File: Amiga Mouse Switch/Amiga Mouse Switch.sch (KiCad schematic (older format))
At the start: 8 parts, among them J1 Joystick 0, J2 Joystick 1, M1 Mounting, M2 Mounting, M3 Mounting, M4 Mounting, M5 Mounting, M6 Mounting

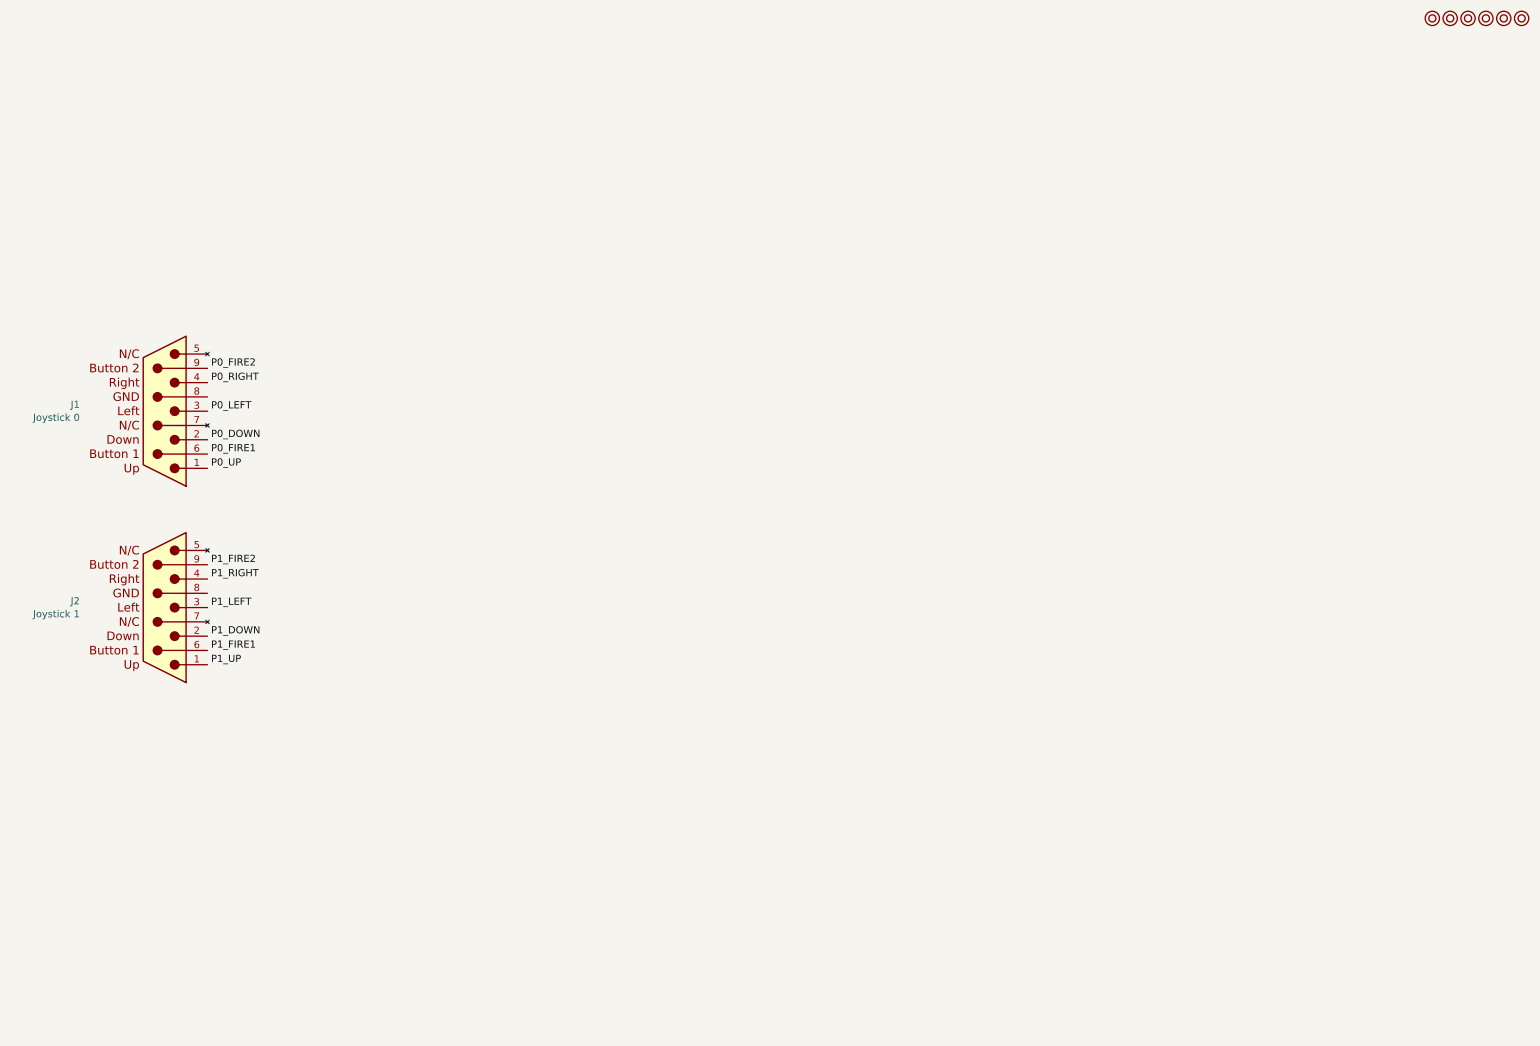
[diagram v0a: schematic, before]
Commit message: Schematic done
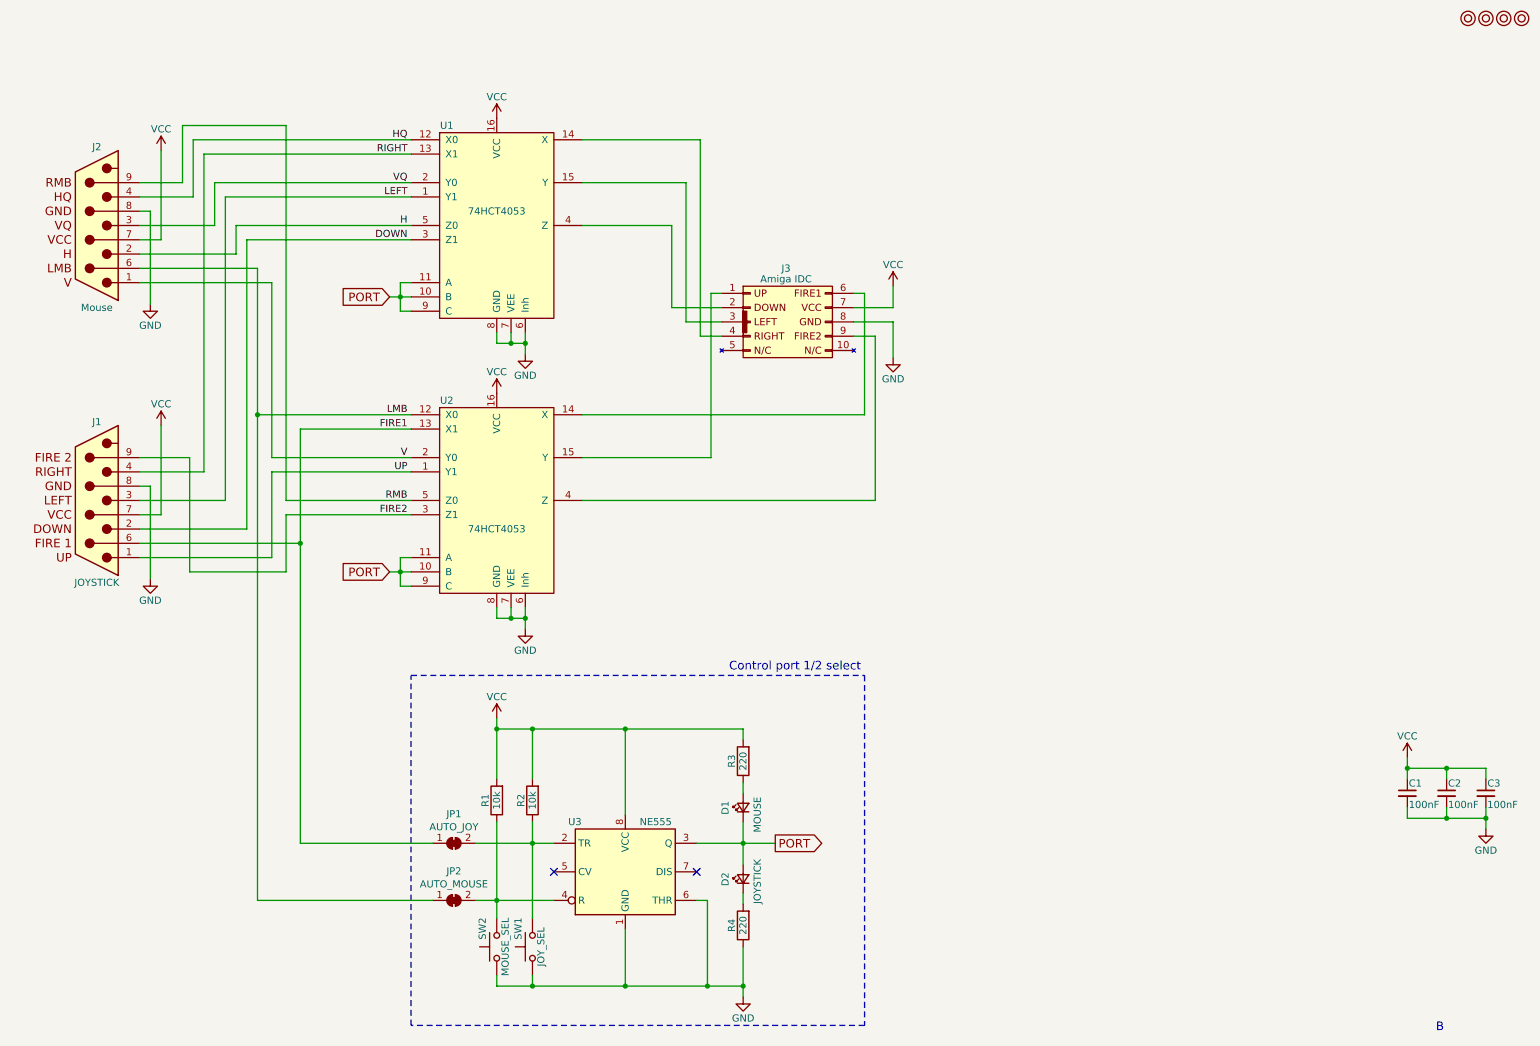
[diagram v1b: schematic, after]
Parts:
- removed J1: Joystick 0, RND:DSUB-9_Male_Horizontal_P2.77x2.84mm_EdgePinOffset7.70mm_Housed_MountingHolesOffset9.12mm, symbol sega_joypad:sms_joypad
- removed J2: Joystick 1, RND:DSUB-9_Male_Horizontal_P2.77x2.84mm_EdgePinOffset7.70mm_Housed_MountingHolesOffset9.12mm, symbol sega_joypad:sms_joypad
- removed M5, M6: Mounting, mounting:M3_pin, symbol mounting:Mounting
- added C1, C2, C3: 100nF, Capacitors_THT:C_Disc_D4.7mm_W2.5mm_P5.00mm, symbol Device:C_Small
- added D1: MOUSE, LEDs:LED_D5.0mm, symbol Device:LED_Small
- added D2: JOYSTICK, LEDs:LED_D5.0mm, symbol Device:LED_Small
- added J1: JOYSTICK, RND:DSUB-9_Male_Horizontal_P2.77x2.84mm_EdgePinOffset7.70mm_Housed_MountingHolesOffset9.12mm, symbol amiga_ports:Amiga_Joystick
- added J2: Mouse, RND:DSUB-9_Male_Horizontal_P2.77x2.84mm_EdgePinOffset7.70mm_Housed_MountingHolesOffset9.12mm, symbol amiga_ports:Amiga_Mouse
- added J3: Amiga IDC, IDC_Joystick:IDC_Joystick, symbol amiga_ports:Amiga_IDC
- added JP1: AUTO_JOY, solder_bridge:bridge, symbol Jumper:SolderJumper_2_Bridged
- added JP2: AUTO_MOUSE, solder_bridge:bridge, symbol Jumper:SolderJumper_2_Bridged
- added R1, R2: 10k, Resistors_THT:R_Axial_DIN0207_L6.3mm_D2.5mm_P10.16mm_Horizontal, symbol Device:R
- added R3, R4: 220, Resistors_THT:R_Axial_DIN0207_L6.3mm_D2.5mm_P10.16mm_Horizontal, symbol Device:R
- added SW1: JOY_SEL, Buttons_Switches_THT:SW_PUSH_6mm, symbol Switch:SW_Push
- added SW2: MOUSE_SEL, Buttons_Switches_THT:SW_PUSH_6mm, symbol Switch:SW_Push
- added U1, U2: 74HCT4053, Housings_DIP:DIP-16_W7.62mm_Socket, symbol 74hct4053:74HCT4053
- added U3: NE555, Housings_DIP:DIP-8_W7.62mm_Socket, symbol Timer:NE555P
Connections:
- new net: J3.4 (Pin_4), U1.14 (X)
- new net: J3.3 (Pin_3), U1.15 (Y)
- new net: J3.2 (Pin_2), U1.4 (Z)
- new net: J3.6 (Pin_6), U2.14 (X)
- new net: J3.1 (Pin_1), U2.15 (Y)
- new net: J3.9 (Pin_9), U2.4 (Z)
- new net: JP1.2 (B), R2.1, SW1.2, U3.2 (TR)
- new net: JP2.2 (B), R1.1, SW2.2, U3.4 (R)
- new net: D2.1 (K), R4.2
- new net: D1.2 (A), R3.1
- new net DOWN: J1.2, U1.3 (Z1)
- new net FIRE1: J1.6, JP1.1 (A), U2.13 (X1)
- new net FIRE2: J1.9, U2.3 (Z1)
- new net GND: C1.2, C2.2, C3.2, J1.8 (GND), J2.8 (GND), J3.8 (Pin_8), R4.1, SW1.1, SW2.1, U1.6 (Inh), U1.7 (VEE), U1.8 (GND), U2.6 (Inh), U2.7 (VEE), U2.8 (GND), U3.1 (GND), U3.6 (THR)
- new net H: J2.2, U1.5 (Z0)
- new net HQ: J2.4, U1.12 (X0)
- new net LEFT: J1.3, U1.1 (Y1)
- new net LMB: J2.6, JP2.1 (A), U2.12 (X0)
- new net PORT: D1.1 (K), D2.2 (A), U1.10 (B), U1.11 (A), U1.9 (C), U2.10 (B), U2.11 (A), U2.9 (C), U3.3 (Q)
- new net RIGHT: J1.4, U1.13 (X1)
- new net RMB: J2.9, U2.5 (Z0)
- new net UP: J1.1, U2.1 (Y1)
- new net V: J2.1, U2.2 (Y0)
- new net VCC: C1.1, C2.1, C3.1, J1.7 (VCC), J2.7 (VCC), J3.7 (Pin_7), R1.2, R2.2, R3.2, U1.16 (VCC), U2.16 (VCC), U3.8 (VCC)
- new net VQ: J2.3, U1.2 (Y0)
- no-connect marks 0 -> 2
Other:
- note added: "B"
- note added: "Control port 1/2 select"

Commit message: Layout done
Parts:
- C1, C2, C3: footprint Capacitors_THT:C_Disc_D4.7mm_W2.5mm_P5.00mm -> Capacitor_THT:C_Disc_D4.7mm_W2.5mm_P5.00mm
- D1, D2: footprint LEDs:LED_D5.0mm -> LED_THT:LED_D5.0mm
- R1, R2, R3, R4: footprint Resistors_THT:R_Axial_DIN0207_L6.3mm_D2.5mm_P10.16mm_Horizontal -> Resistor_THT:R_Axial_DIN0207_L6.3mm_D2.5mm_P10.16mm_Horizontal
- SW1, SW2: footprint Buttons_Switches_THT:SW_PUSH_6mm -> switch_cutout:SW_PUSH_6mm
- U1, U2: footprint Housings_DIP:DIP-16_W7.62mm_Socket -> Package_DIP:DIP-16_W7.62mm_Socket_LongPads
- U3: footprint Housings_DIP:DIP-8_W7.62mm_Socket -> Package_DIP:DIP-8_W7.62mm_Socket_LongPads
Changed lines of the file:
@@
 F 0 "U3" H 4475 6875 50  0000 L CNN
 F 1 "NE555" H 4975 6875 50  0000 L CNN
-F 2 "Housings_DIP:DIP-8_W7.62mm_Socket" H 4875 6525 50  0001 C CNN
+F 2 "Package_DIP:DIP-8_W7.62mm_Socket_LongPads" H 4875 6525 50  0001 C CNN
 F 3 "" H 4875 6525 50  0001 C CNN
 	1    4875 6525
@@
 F 0 "R2" V 4305 6025 50  0000 C CNN
 F 1 "10k" V 4225 6025 50  0000 C CNN
-F 2 "Resistors_THT:R_Axial_DIN0207_L6.3mm_D2.5mm_P10.16mm_Horizontal" V 4155 6025 50  0001 C CNN
+F 2 "Resistor_THT:R_Axial_DIN0207_L6.3mm_D2.5mm_P10.16mm_Horizontal" V 4155 6025 50  0001 C CNN
 F 3 "" H 4225 6025 50  0001 C CNN
 	1    4225 6025
@@
 F 0 "R1" V 4055 6025 50  0000 C CNN
 F 1 "10k" V 3975 6025 50  0000 C CNN
-F 2 "Resistors_THT:R_Axial_DIN0207_L6.3mm_D2.5mm_P10.16mm_Horizontal" V 3905 6025 50  0001 C CNN
+F 2 "Resistor_THT:R_Axial_DIN0207_L6.3mm_D2.5mm_P10.16mm_Horizontal" V 3905 6025 50  0001 C CNN
 F 3 "" H 3975 6025 50  0001 C CNN
 	1    3975 6025
@@
 F 0 "SW1" H 4275 7150 50  0000 L CNN
 F 1 "JOY_SEL" H 4225 6990 50  0000 C CNN
-F 2 "Buttons_Switches_THT:SW_PUSH_6mm" H 4225 7250 50  0001 C CNN
+F 2 "switch_cutout:SW_PUSH_6mm" H 4225 7250 50  0001 C CNN
 F 3 "" H 4225 7250 50  0001 C CNN
 	1    4225 7050
@@
 F 0 "SW2" H 4025 7150 50  0000 L CNN
 F 1 "MOUSE_SEL" H 3975 6990 50  0000 C CNN
-F 2 "Buttons_Switches_THT:SW_PUSH_6mm" H 3975 7250 50  0001 C CNN
+F 2 "switch_cutout:SW_PUSH_6mm" H 3975 7250 50  0001 C CNN
 F 3 "" H 3975 7250 50  0001 C CNN
 	1    3975 7050
@@
 F 0 "R4" V 5780 6900 50  0000 C CNN
 F 1 "220" V 5700 6900 50  0000 C CNN
-F 2 "Resistors_THT:R_Axial_DIN0207_L6.3mm_D2.5mm_P10.16mm_Horizontal" V 5630 6900 50  0001 C CNN
+F 2 "Resistor_THT:R_Axial_DIN0207_L6.3mm_D2.5mm_P10.16mm_Horizontal" V 5630 6900 50  0001 C CNN
 F 3 "" H 5700 6900 50  0001 C CNN
 	1    5700 6900
@@
 F 0 "D1" H 5650 6200 50  0000 L CNN
 F 1 "MOUSE" H 5525 5975 50  0000 L CNN
-F 2 "LEDs:LED_D5.0mm" V 5700 6075 50  0001 C CNN
+F 2 "LED_THT:LED_D5.0mm" V 5700 6075 50  0001 C CNN
 F 3 "" V 5700 6075 50  0001 C CNN
 	1    5700 6075
@@
 F 0 "D2" H 5650 6700 50  0000 L CNN
 F 1 "JOYSTICK" H 5525 6475 50  0000 L CNN
-F 2 "LEDs:LED_D5.0mm" V 5700 6575 50  0001 C CNN
+F 2 "LED_THT:LED_D5.0mm" V 5700 6575 50  0001 C CNN
 F 3 "" V 5700 6575 50  0001 C CNN
 	1    5700 6575
@@
 F 0 "R3" V 5780 5750 50  0000 C CNN
 F 1 "220" V 5700 5750 50  0000 C CNN
-F 2 "Resistors_THT:R_Axial_DIN0207_L6.3mm_D2.5mm_P10.16mm_Horizontal" V 5630 5750 50  0001 C CNN
+F 2 "Resistor_THT:R_Axial_DIN0207_L6.3mm_D2.5mm_P10.16mm_Horizontal" V 5630 5750 50  0001 C CNN
 F 3 "" H 5700 5750 50  0001 C CNN
 	1    5700 5750
@@
 F 0 "C1" H 10360 6045 50  0000 L CNN
 F 1 "100nF" H 10360 5895 50  0000 L CNN
-F 2 "Capacitors_THT:C_Disc_D4.7mm_W2.5mm_P5.00mm" H 10350 5975 50  0001 C CNN
+F 2 "Capacitor_THT:C_Disc_D4.7mm_W2.5mm_P5.00mm" H 10350 5975 50  0001 C CNN
 F 3 "" H 10350 5975 50  0001 C CNN
 	1    10350 5975
@@
 F 0 "C2" H 10635 6045 50  0000 L CNN
 F 1 "100nF" H 10635 5895 50  0000 L CNN
-F 2 "Capacitors_THT:C_Disc_D4.7mm_W2.5mm_P5.00mm" H 10625 5975 50  0001 C CNN
+F 2 "Capacitor_THT:C_Disc_D4.7mm_W2.5mm_P5.00mm" H 10625 5975 50  0001 C CNN
 F 3 "" H 10625 5975 50  0001 C CNN
 	1    10625 5975
@@
 F 0 "C3" H 10910 6045 50  0000 L CNN
 F 1 "100nF" H 10910 5895 50  0000 L CNN
-F 2 "Capacitors_THT:C_Disc_D4.7mm_W2.5mm_P5.00mm" H 10900 5975 50  0001 C CNN
+F 2 "Capacitor_THT:C_Disc_D4.7mm_W2.5mm_P5.00mm" H 10900 5975 50  0001 C CNN
 F 3 "" H 10900 5975 50  0001 C CNN
 	1    10900 5975
@@
 F 0 "U1" H 3625 2700 50  0000 C CNN
 F 1 "74HCT4053" H 3975 2100 50  0000 C CNN
-F 2 "Housings_DIP:DIP-16_W7.62mm_Socket" H 3975 2000 60  0001 C CNN
+F 2 "Package_DIP:DIP-16_W7.62mm_Socket_LongPads" H 3975 2000 60  0001 C CNN
 F 3 "" H 3975 2000 60  0001 C CNN
 	1    3975 2000
@@
 F 0 "U2" H 3625 4625 50  0000 C CNN
 F 1 "74HCT4053" H 3975 3725 50  0000 C CNN
-F 2 "Housings_DIP:DIP-16_W7.62mm_Socket" H 3975 3925 60  0001 C CNN
+F 2 "Package_DIP:DIP-16_W7.62mm_Socket_LongPads" H 3975 3925 60  0001 C CNN
 F 3 "" H 3975 3925 60  0001 C CNN
 	1    3975 3925

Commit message: Gerber export
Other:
- note removed: "B"
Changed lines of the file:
@@
 Comment2 ""
 Comment3 ""
-Comment4 "Simple port switcher, change active device by pushing one of the buttons."
+Comment4 "Simple port switcher, change active device by pushing FIRE1/LMB."
 $EndDescr
 $Comp
@@
 	1    0    0    -1
 $EndComp
-Text Notes 10550 7650 0    60   ~ 0
-B
 Wire Wire Line
 	1475 3725 1925 3725
